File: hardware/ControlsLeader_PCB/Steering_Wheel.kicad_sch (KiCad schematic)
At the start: 6 parts, among them J10 Indicator_Switch, Q6 NMOS

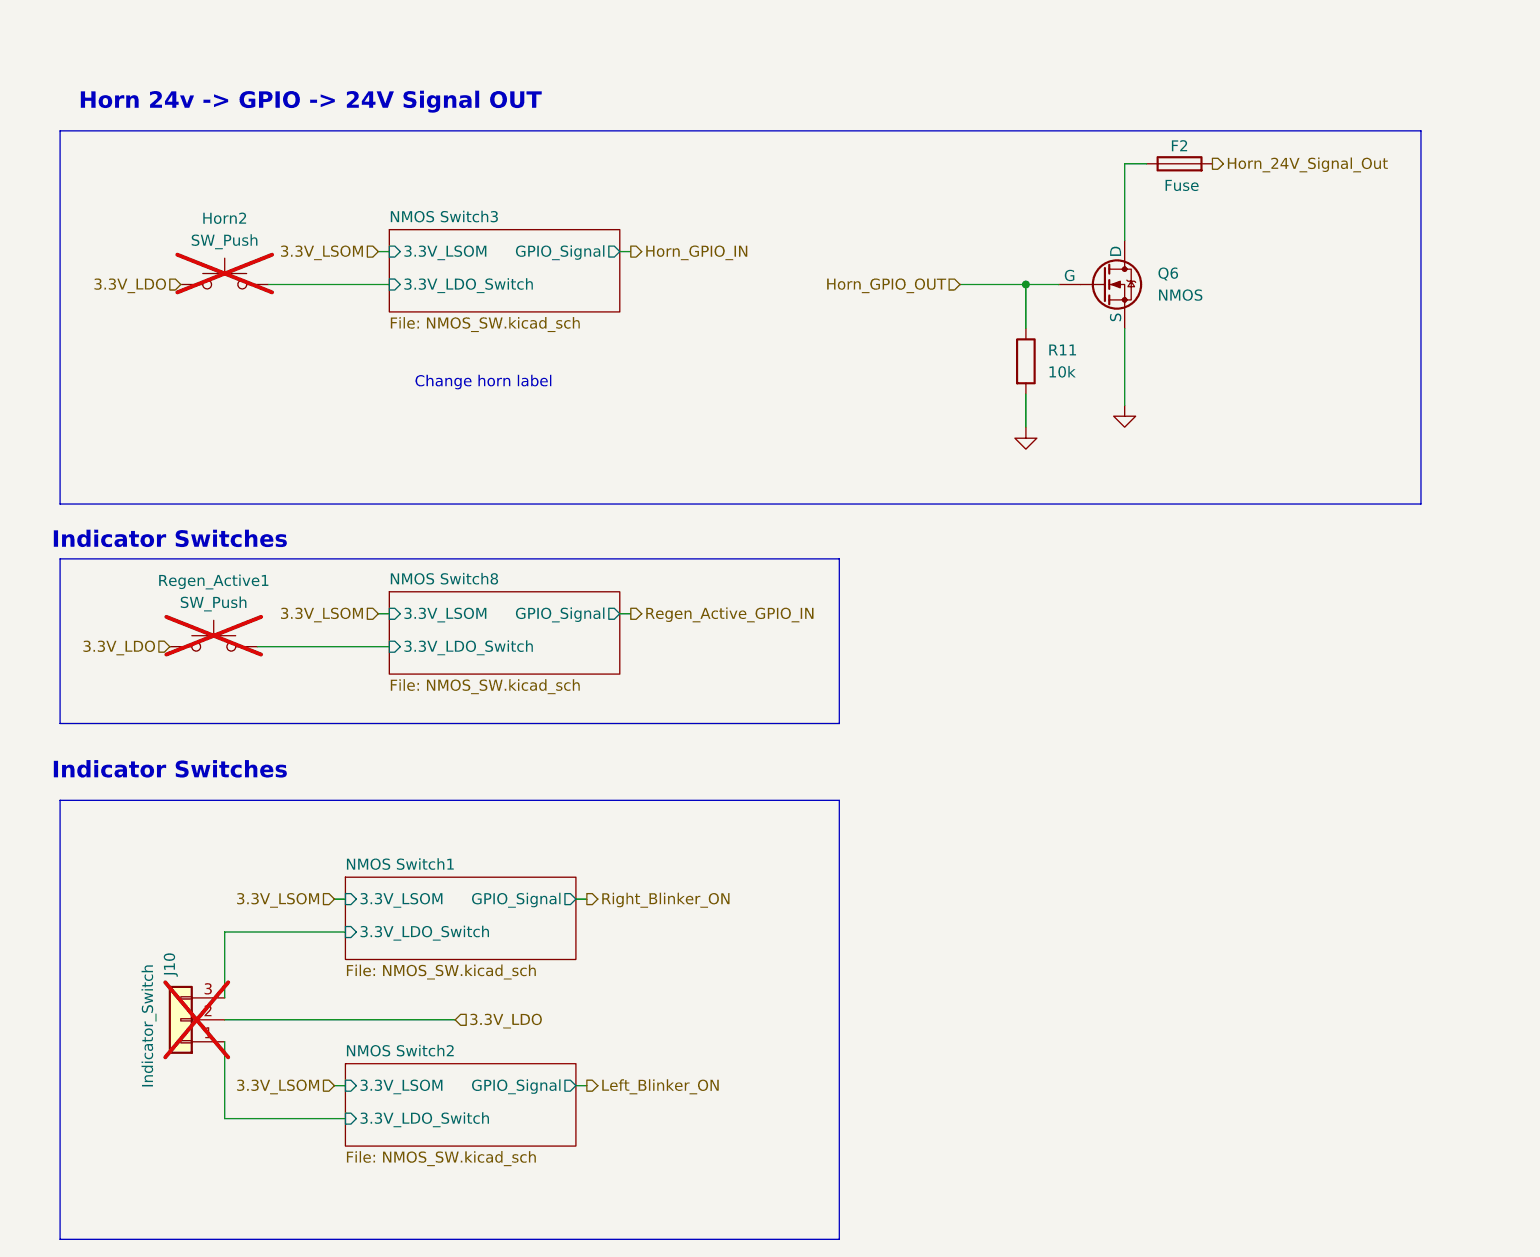
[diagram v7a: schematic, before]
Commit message: PCB DESIGN DONE - need to add datasheets and p/n
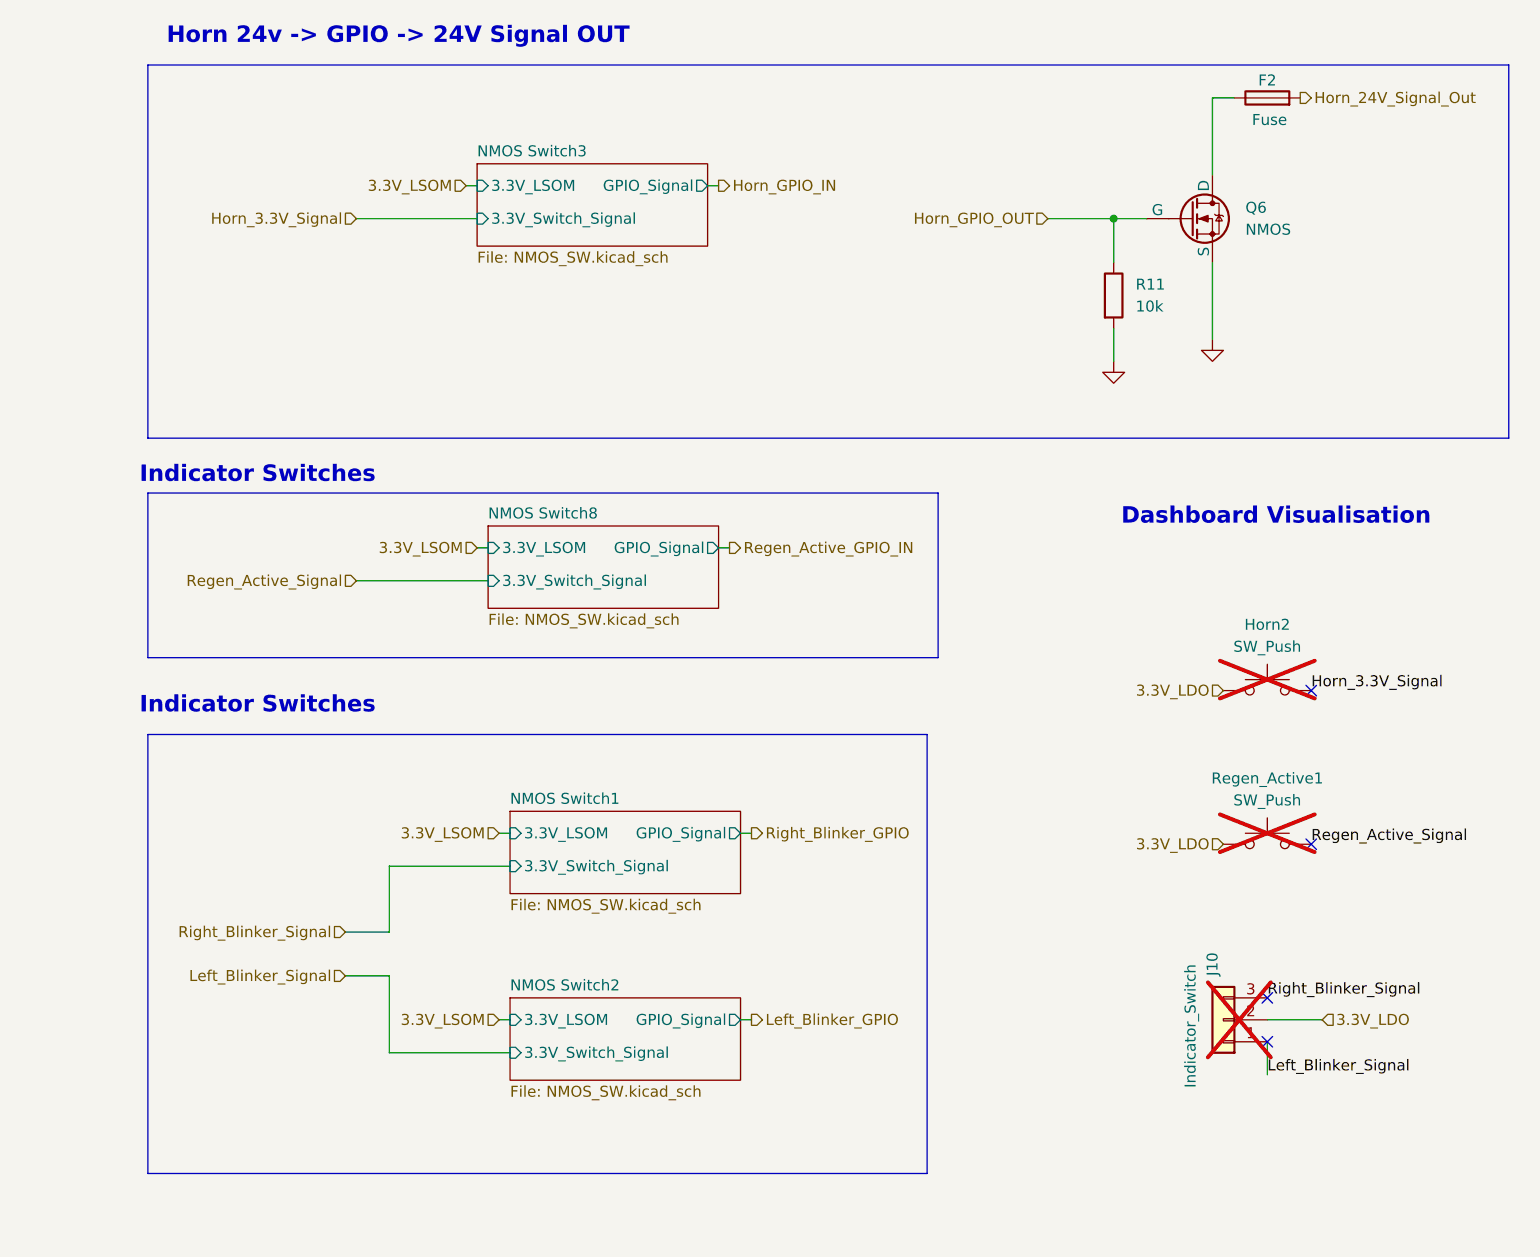
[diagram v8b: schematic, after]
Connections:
- net NMOS Switch1/3.3V_LDO_Switch renamed Right_Blinker_Signal
- net NMOS Switch2/3.3V_LDO_Switch renamed Left_Blinker_Signal
- net NMOS Switch3/3.3V_LDO_Switch renamed Horn_3.3V_Signal
- net NMOS Switch8/3.3V_LDO_Switch renamed Regen_Active_Signal
- no-connect marks 0 -> 4
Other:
- sheet NMOS Switch1 ports: added 3.3V_Switch_Signal; removed 3.3V_LDO_Switch
- sheet NMOS Switch2 ports: added 3.3V_Switch_Signal; removed 3.3V_LDO_Switch
- sheet NMOS Switch3 ports: added 3.3V_Switch_Signal; removed 3.3V_LDO_Switch
- sheet NMOS Switch8 ports: added 3.3V_Switch_Signal; removed 3.3V_LDO_Switch
- note added: "Dashboard Visualisation"
- note removed: "Change horn label"
- moved on the sheet: F2, Horn2, J10, Q6, R11, Regen_Active1
